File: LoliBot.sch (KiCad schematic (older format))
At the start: 37 parts, among them J1 LOLINBATT, J10 LEFT-MOTOR, J11 REFLECT_, J12 MECH, J13 MECH, J14 MECH, J15 MECH, J16 MECH, J17 MECH, J18 MECH, J19 MECH, J2 APA106, J3 SERVO1, J4 RIGHT, J5 LEFT, J6 MPU-9250, J7 APA106, J8 APA106, J9 RIGHT-MOTOR, SW1 SPST, U1 LOLIN32-LITE, U2 RT9276, U3 L9110, U4 L9110

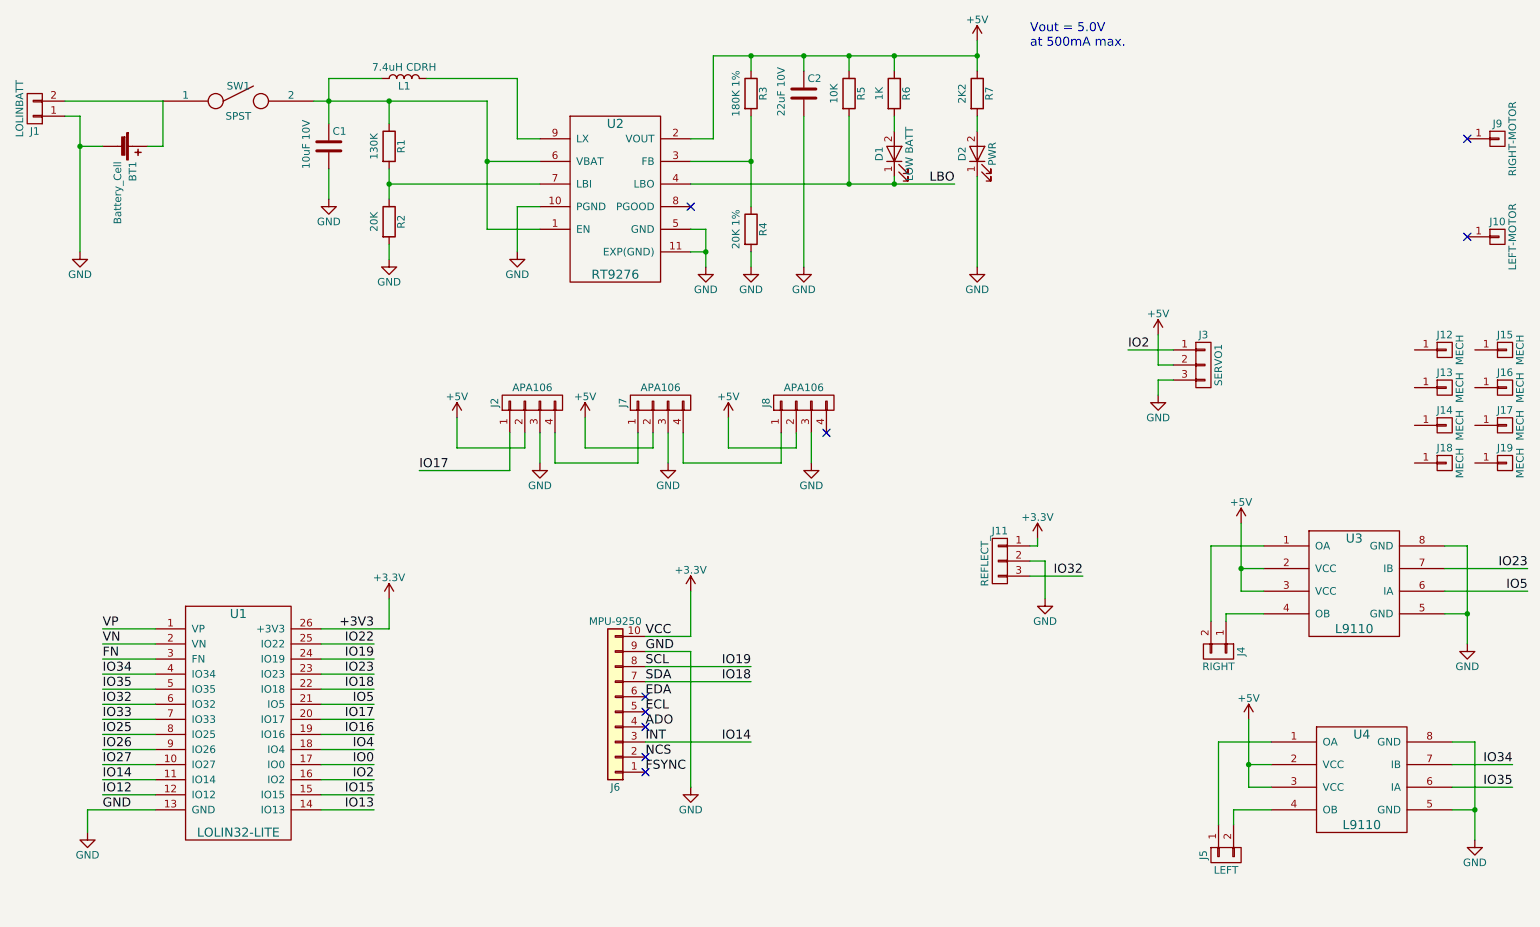
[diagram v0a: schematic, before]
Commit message: Pin reassignment.
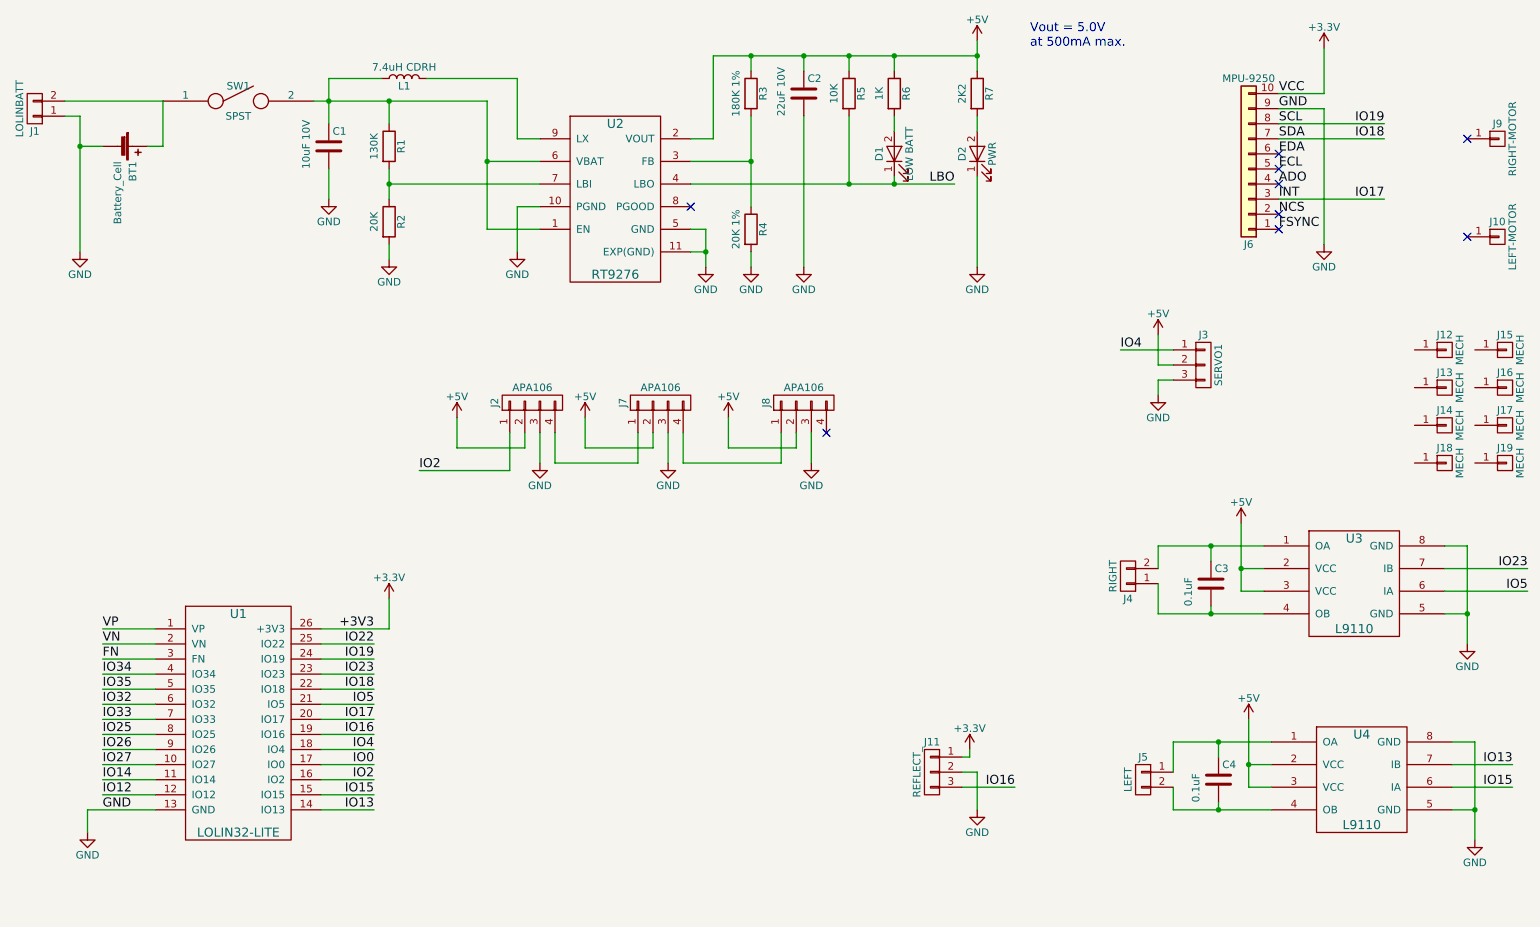
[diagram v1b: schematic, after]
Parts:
- added C3, C4: 0.1uF, Capacitors_SMD:C_0805_HandSoldering, symbol C
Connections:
- net INT: now also U1.20 (IO17); no longer U1.11 (IO14)
- net IO13: now also U4.7 (IB)
- net IO15: now also U4.6 (IA)
- net IO16: now also J11.3 (P3)
- net IO2: now also J2.1 (P1); no longer J3.1 (P1)
- net IO32: no longer J11.3 (P3)
- net IO34: no longer U4.7 (IB)
- net IO35: no longer U4.6 (IA)
- net IO4: now also J3.1 (P1)
- net at J4.2 (P2), U3.1 (OA): now also C3.1
- net at J4.1 (P1), U3.4 (OB): now also C3.2
- net at J5.1 (P1), U4.1 (OA): now also C4.1
- net at J5.2 (P2), U4.4 (OB): now also C4.2
- removed net IO17: J2.1 (P1), U1.20 (IO17)
- new net IO14: U1.11 (IO14)
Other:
- moved on the sheet: J11, J4, J5, J6
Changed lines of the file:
@@
 L CONN_01X02 J4
 U 1 1 59DBB5AA
-P 8800 4800
-F 0 "J4" H 8800 4950 50  0000 C CNN
-F 1 "RIGHT" V 8900 4800 50  0000 C CNN
-F 2 "Pin_Headers:Pin_Header_Straight_1x02_Pitch2.00mm" H 8800 4800 50  0001 C CNN
-F 3 "" H 8800 4800 50  0001 C CNN
-	1    8800 4800
-	0    1    1    0
+P 8200 4300
+F 0 "J4" H 8200 4450 50  0000 C CNN
+F 1 "RIGHT" V 8300 4300 50  0000 C CNN
+F 2 "Pin_Headers:Pin_Header_Straight_1x02_Pitch2.00mm" H 8200 4300 50  0001 C CNN
+F 3 "" H 8200 4300 50  0001 C CNN
+	1    8200 4300
+	-1   0    0    1
 $EndComp
 $Comp
@@
 L CONN_01X02 J5
 U 1 1 59DBCDBD
-P 8850 6150
-F 0 "J5" H 8850 6300 50  0000 C CNN
-F 1 "LEFT" V 8950 6150 50  0000 C CNN
-F 2 "Pin_Headers:Pin_Header_Straight_1x02_Pitch2.00mm" H 8850 6150 50  0001 C CNN
-F 3 "" H 8850 6150 50  0001 C CNN
-	1    8850 6150
-	0    -1   1    0
+P 8300 5650
+F 0 "J5" H 8300 5800 50  0000 C CNN
+F 1 "LEFT" V 8400 5650 50  0000 C CNN
+F 2 "Pin_Headers:Pin_Header_Straight_1x02_Pitch2.00mm" H 8300 5650 50  0001 C CNN
+F 3 "" H 8300 5650 50  0001 C CNN
+	1    8300 5650
+	-1   0    0    -1
 $EndComp
 $Comp
@@
 	9150 5550 9000 5550
 Connection ~ 9000 5550
-Text Label 10750 5550 2    60   ~ 0
-IO34
-Text Label 10750 5700 2    60   ~ 0
-IO35
 $Comp
 L CONN_01X03 J3
@@
 	8400 3000 8500 3000
 Wire Wire Line
-	8500 2800 8200 2800
-Text Label 8200 2800 0    60   ~ 0
-IO2
+	8500 2800 8150 2800
 Wire Wire Line
 	1750 4650 1400 4650
@@
 L Conn_01x10 J6
 U 1 1 59E28CBB
-P 4800 5200
-F 0 "J6" H 4800 5700 50  0000 C CNN
-F 1 "MPU-9250" H 4800 4600 50  0000 C CNN
-F 2 "Pin_Headers:Pin_Header_Straight_1x10_Pitch2.54mm" H 4800 5200 50  0001 C CNN
-F 3 "" H 4800 5200 50  0001 C CNN
-	1    4800 5200
+P 9000 1600
+F 0 "J6" H 9000 2100 50  0000 C CNN
+F 1 "MPU-9250" H 9000 1000 50  0000 C CNN
+F 2 "Pin_Headers:Pin_Header_Straight_1x10_Pitch2.54mm" H 9000 1600 50  0001 C CNN
+F 3 "" H 9000 1600 50  0001 C CNN
+	1    9000 1600
 	-1   0    0    1
 $EndComp
-Text Label 5000 4700 0    60   ~ 0
+Text Label 9200 1100 0    60   ~ 0
 VCC
-Text Label 5000 4800 0    60   ~ 0
+Text Label 9200 1200 0    60   ~ 0
 GND
-Text Label 5000 4900 0    60   ~ 0
+Text Label 9200 1300 0    60   ~ 0
 SCL
-Text Label 5000 5000 0    60   ~ 0
+Text Label 9200 1400 0    60   ~ 0
 SDA
-Text Label 5000 5100 0    60   ~ 0
+Text Label 9200 1500 0    60   ~ 0
 EDA
-Text Label 5000 5200 0    60   ~ 0
+Text Label 9200 1600 0    60   ~ 0
 ECL
-Text Label 5000 5300 0    60   ~ 0
+Text Label 9200 1700 0    60   ~ 0
 ADO
-Text Label 5000 5400 0    60   ~ 0
+Text Label 9200 1800 0    60   ~ 0
 INT
-Text Label 5000 5500 0    60   ~ 0
+Text Label 9200 1900 0    60   ~ 0
 NCS
-Text Label 5000 5600 0    60   ~ 0
+Text Label 9200 2000 0    60   ~ 0
 FSYNC
 $Comp
 L +3.3V #PWR020
 U 1 1 59E28F97
-P 5300 4400
-F 0 "#PWR020" H 5300 4250 50  0001 C CNN
-F 1 "+3.3V" H 5300 4540 50  0000 C CNN
-F 2 "" H 5300 4400 50  0001 C CNN
-F 3 "" H 5300 4400 50  0001 C CNN
-	1    5300 4400
-	1    0    0    -1
-$EndComp
-Wire Wire Line
-	5000 4700 5300 4700
-Wire Wire Line
-	5300 4700 5300 4400
+P 9500 800
+F 0 "#PWR020" H 9500 650 50  0001 C CNN
+F 1 "+3.3V" H 9500 940 50  0000 C CNN
+F 2 "" H 9500 800 50  0001 C CNN
+F 3 "" H 9500 800 50  0001 C CNN
+	1    9500 800
+	1    0    0    -1
+$EndComp
+Wire Wire Line
+	9200 1100 9500 1100
+Wire Wire Line
+	9500 1100 9500 800
 $Comp
 L GND #PWR021
 U 1 1 59E29073
-P 5300 5700
-F 0 "#PWR021" H 5300 5450 50  0001 C CNN
-F 1 "GND" H 5300 5550 50  0000 C CNN
-F 2 "" H 5300 5700 50  0001 C CNN
-F 3 "" H 5300 5700 50  0001 C CNN
-	1    5300 5700
-	1    0    0    -1
-$EndComp
-Wire Wire Line
-	5000 4800 5300 4800
-Wire Wire Line
-	5300 4800 5300 5700
-Wire Wire Line
-	5000 4900 5700 4900
-Wire Wire Line
-	5000 5000 5700 5000
-Text Label 5700 4900 2    60   ~ 0
+P 9500 2100
+F 0 "#PWR021" H 9500 1850 50  0001 C CNN
+F 1 "GND" H 9500 1950 50  0000 C CNN
+F 2 "" H 9500 2100 50  0001 C CNN
+F 3 "" H 9500 2100 50  0001 C CNN
+	1    9500 2100
+	1    0    0    -1
+$EndComp
+Wire Wire Line
+	9200 1200 9500 1200
+Wire Wire Line
+	9500 1200 9500 2100
+Wire Wire Line
+	9200 1300 9900 1300
+Wire Wire Line
+	9200 1400 9900 1400
+Text Label 9900 1300 2    60   ~ 0
 IO19
-Text Label 5700 5000 2    60   ~ 0
+Text Label 9900 1400 2    60   ~ 0
 IO18
 Wire Wire Line
-	5000 5400 5700 5400
-Text Label 5700 5400 2    60   ~ 0
-IO14
-NoConn ~ 5000 5600
-NoConn ~ 5000 5500
-NoConn ~ 5000 5300
-NoConn ~ 5000 5200
-NoConn ~ 5000 5100
+	9200 1800 9900 1800
+NoConn ~ 9200 2000
+NoConn ~ 9200 1900
+NoConn ~ 9200 1700
+NoConn ~ 9200 1600
+NoConn ~ 9200 1500
 $Comp
 L CONN_01X04 J7
@@
 Wire Wire Line
 	3500 3600 4100 3600
-Text Label 3500 3600 0    60   ~ 0
-IO17
 $Comp
 L +5V #PWR022
@@
 L CONN_01X03 J11
 U 1 1 59F9CFA7
-P 7350 4200
-F 0 "J11" H 7350 4400 50  0000 C CNN
-F 1 "REFLECT_" V 7450 4200 50  0000 C CNN
-F 2 "Pin_Headers:Pin_Header_Straight_1x03_Pitch2.54mm" H 7350 4200 50  0001 C CNN
-F 3 "" H 7350 4200 50  0001 C CNN
-	1    7350 4200
+P 6900 5600
+F 0 "J11" H 6900 5800 50  0000 C CNN
+F 1 "REFLECT_" V 7000 5600 50  0000 C CNN
+F 2 "Pin_Headers:Pin_Header_Straight_1x03_Pitch2.54mm" H 6900 5600 50  0001 C CNN
+F 3 "" H 6900 5600 50  0001 C CNN
+	1    6900 5600
 	-1   0    0    -1
 $EndComp
@@
 L +3.3V #PWR026
 U 1 1 59F9D53B
-P 7600 4050
-F 0 "#PWR026" H 7600 3900 50  0001 C CNN
-F 1 "+3.3V" H 7600 4190 50  0000 C CNN
-F 2 "" H 7600 4050 50  0001 C CNN
-F 3 "" H 7600 4050 50  0001 C CNN
-	1    7600 4050
+P 7150 5450
+F 0 "#PWR026" H 7150 5300 50  0001 C CNN
+F 1 "+3.3V" H 7150 5590 50  0000 C CNN
+F 2 "" H 7150 5450 50  0001 C CNN
+F 3 "" H 7150 5450 50  0001 C CNN
+	1    7150 5450
 	1    0    0    -1
 $EndComp
@@
 L GND #PWR027
 U 1 1 59F9DB04
-P 7650 4450
-F 0 "#PWR027" H 7650 4200 50  0001 C CNN
-F 1 "GND" H 7650 4300 50  0000 C CNN
-F 2 "" H 7650 4450 50  0001 C CNN
-F 3 "" H 7650 4450 50  0001 C CNN
-	1    7650 4450
-	1    0    0    -1
-$EndComp
-Wire Wire Line
-	7550 4100 7600 4100
-Wire Wire Line
-	7600 4100 7600 4050
-Wire Wire Line
-	7550 4200 7650 4200
-Wire Wire Line
-	7650 4200 7650 4450
-Text Label 7900 4300 2    60   ~ 0
-IO32
-Wire Wire Line
-	7550 4300 7900 4300
+P 7200 5850
+F 0 "#PWR027" H 7200 5600 50  0001 C CNN
+F 1 "GND" H 7200 5700 50  0000 C CNN
+F 2 "" H 7200 5850 50  0001 C CNN
+F 3 "" H 7200 5850 50  0001 C CNN
+	1    7200 5850
+	1    0    0    -1
+$EndComp
+Wire Wire Line
+	7100 5500 7150 5500
+Wire Wire Line
+	7150 5500 7150 5450
+Wire Wire Line
+	7100 5600 7200 5600
+Wire Wire Line
+	7200 5600 7200 5850
+Wire Wire Line
+	7100 5700 7450 5700
 $Comp
 L CONN_01X01 J19
@@
 $EndComp
 Wire Wire Line
-	8850 4600 8850 4550
-Wire Wire Line
-	8850 4550 9100 4550
-Wire Wire Line
-	9100 4100 8750 4100
-Wire Wire Line
-	8750 4100 8750 4600
-Wire Wire Line
-	9150 5850 8900 5850
-Wire Wire Line
-	8900 5850 8900 5950
-Wire Wire Line
-	9150 5400 8800 5400
-Wire Wire Line
-	8800 5400 8800 5950
+	8400 4550 9100 4550
+Wire Wire Line
+	8400 4100 9100 4100
+Wire Wire Line
+	8500 5850 9150 5850
+Wire Wire Line
+	8500 5400 9150 5400
+Text Label 10750 5550 2    60   ~ 0
+IO13
+Text Label 9900 1800 2    60   ~ 0
+IO17
+Text Label 7450 5700 2    60   ~ 0
+IO16
+Text Label 8150 2800 0    60   ~ 0
+IO4
+Text Label 3500 3600 0    60   ~ 0
+IO2
+Text Label 10750 5700 2    60   ~ 0
+IO15
+$Comp
+L C C3
+U 1 1 5A0F0864
+P 8750 4350
+F 0 "C3" H 8775 4450 50  0000 L CNN
+F 1 "0.1uF" V 8600 4200 50  0000 L CNN
+F 2 "Capacitors_SMD:C_0805_HandSoldering" H 8788 4200 50  0001 C CNN
+F 3 "" H 8750 4350 50  0001 C CNN
+	1    8750 4350
+	1    0    0    -1
+$EndComp
+$Comp
+L C C4
+U 1 1 5A0F0D3D
+P 8800 5650
+F 0 "C4" H 8825 5750 50  0000 L CNN
+F 1 "0.1uF" V 8650 5500 50  0000 L CNN
+F 2 "Capacitors_SMD:C_0805_HandSoldering" H 8838 5500 50  0001 C CNN
+F 3 "" H 8800 5650 50  0001 C CNN
+	1    8800 5650
+	1    0    0    -1
+$EndComp
+Wire Wire Line
+	8800 5400 8800 5500
+Wire Wire Line
+	8800 5850 8800 5800
+Wire Wire Line
+	8500 5850 8500 5700
+Connection ~ 8800 5850
+Wire Wire Line
+	8500 5400 8500 5600
+Connection ~ 8800 5400
+Wire Wire Line
+	8750 4500 8750 4550
+Wire Wire Line
+	8750 4100 8750 4200
+Wire Wire Line
+	8400 4250 8400 4100
+Connection ~ 8750 4100
+Wire Wire Line
+	8400 4350 8400 4550
+Connection ~ 8750 4550
 $EndSCHEMATC

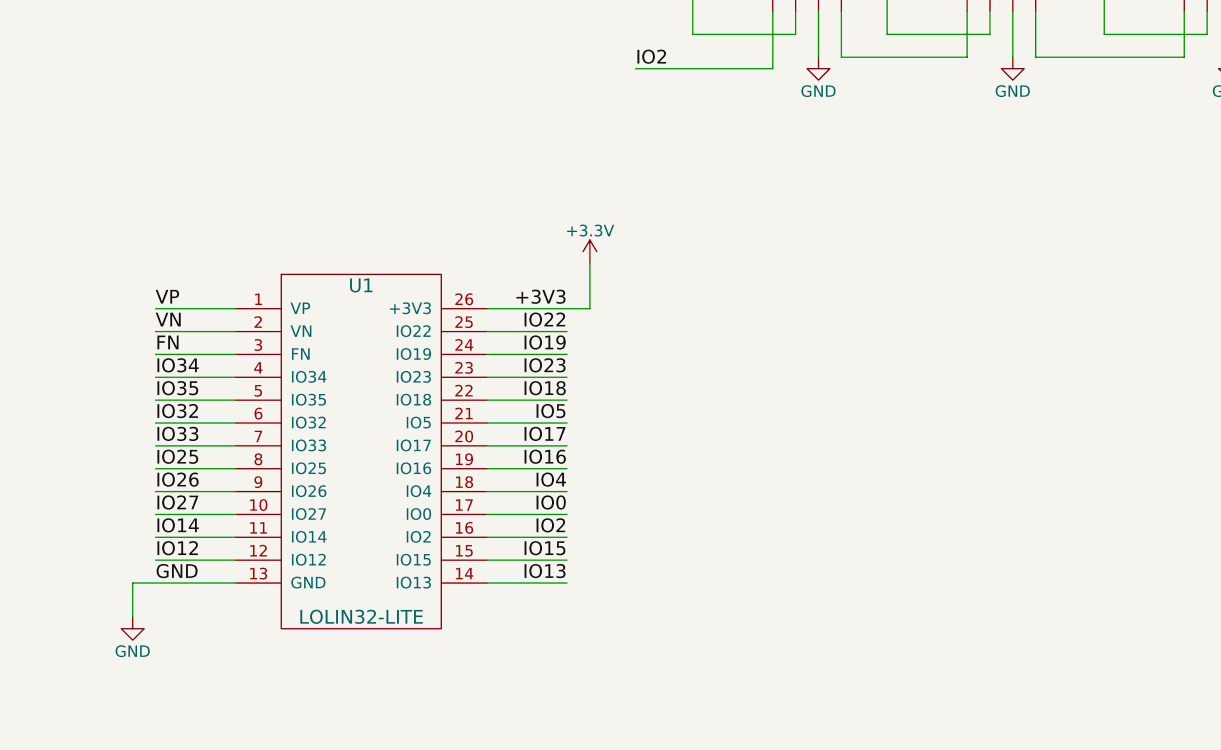
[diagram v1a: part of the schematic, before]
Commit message: Added expansion ports
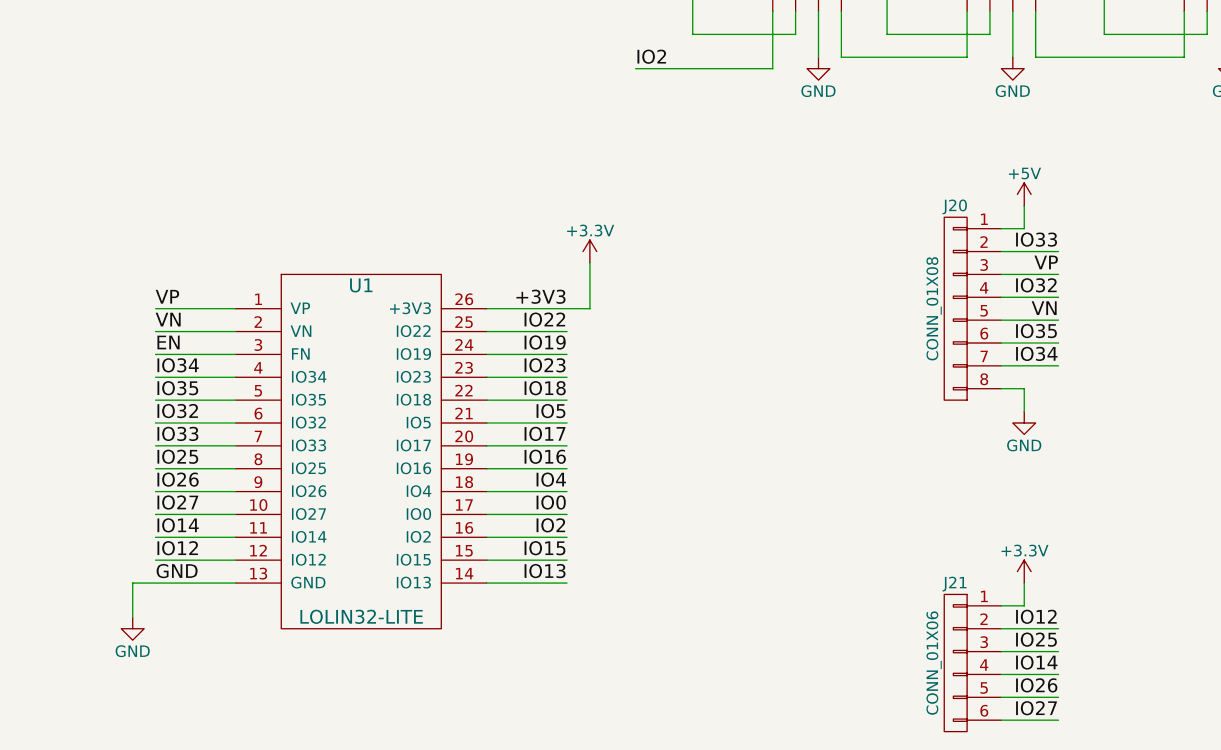
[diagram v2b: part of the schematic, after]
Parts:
- added J20: CONN_01X08, Pin_Headers:Pin_Header_Straight_2x04_Pitch2.54mm, symbol CONN_01X08
- added J21: CONN_01X06, Pin_Headers:Pin_Header_Straight_2x03_Pitch2.54mm, symbol CONN_01X06
- U3, U4: footprint Housings_DIP:DIP-8_W7.62mm -> Housings_SOIC:SOIC-8_3.9x4.9mm_Pitch1.27mm
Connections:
- net +3V3: now also J21.1 (P1)
- net +5V: now also J20.1 (P1)
- net GND: now also J20.8 (P8)
- net IO12: now also J21.2 (P2)
- net IO14: now also J21.4 (P4)
- net IO25: now also J21.3 (P3)
- net IO26: now also J21.5 (P5)
- net IO27: now also J21.6 (P6)
- net IO32: now also J20.4 (P4)
- net IO33: now also J20.2 (P2)
- net IO34: now also J20.7 (P7)
- net IO35: now also J20.6 (P6)
- net VN: now also J20.5 (P5)
- net VP: now also J20.3 (P3)
- net FN renamed EN
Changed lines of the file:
@@
 F 0 "U3" H 9700 4550 60  0000 C CNN
 F 1 "L9110" H 9700 3950 60  0000 C CNN
-F 2 "Housings_DIP:DIP-8_W7.62mm" H 9700 4300 60  0001 C CNN
+F 2 "Housings_SOIC:SOIC-8_3.9x4.9mm_Pitch1.27mm" H 9700 4300 60  0001 C CNN
 F 3 "" H 9700 4300 60  0000 C CNN
 	1    9700 4300
@@
 F 0 "U4" H 9750 5850 60  0000 C CNN
 F 1 "L9110" H 9750 5250 60  0000 C CNN
-F 2 "Housings_DIP:DIP-8_W7.62mm" H 9750 5600 60  0001 C CNN
+F 2 "Housings_SOIC:SOIC-8_3.9x4.9mm_Pitch1.27mm" H 9750 5600 60  0001 C CNN
 F 3 "" H 9750 5600 60  0000 C CNN
 	1    9750 5600
@@
 	1750 4850 1400 4850
 Text Label 1400 4850 0    60   ~ 0
-FN
+EN
 Wire Wire Line
 	1750 4950 1400 4950
@@
 	8400 4350 8400 4550
 Connection ~ 8750 4550
+$Comp
+L CONN_01X08 J20
+U 1 1 5A117712
+P 4900 4650
+F 0 "J20" H 4900 5100 50  0000 C CNN
+F 1 "CONN_01X08" V 5000 4650 50  0000 C CNN
+F 2 "Pin_Headers:Pin_Header_Straight_2x04_Pitch2.54mm" H 4900 4650 50  0001 C CNN
+F 3 "" H 4900 4650 50  0001 C CNN
+	1    4900 4650
+	-1   0    0    -1
+$EndComp
+$Comp
+L +3.3V #PWR028
+U 1 1 5A117D1F
+P 5200 5850
+F 0 "#PWR028" H 5200 5700 50  0001 C CNN
+F 1 "+3.3V" H 5200 5990 50  0000 C CNN
+F 2 "" H 5200 5850 50  0001 C CNN
+F 3 "" H 5200 5850 50  0001 C CNN
+	1    5200 5850
+	1    0    0    -1
+$EndComp
+Wire Wire Line
+	5100 4300 5200 4300
+Wire Wire Line
+	5200 4300 5200 4200
+Text Label 5350 4500 2    60   ~ 0
+VP
+Text Label 5350 4700 2    60   ~ 0
+VN
+Text Label 5350 4900 2    60   ~ 0
+IO34
+Text Label 5350 4800 2    60   ~ 0
+IO35
+Text Label 5350 4600 2    60   ~ 0
+IO32
+Text Label 5350 4400 2    60   ~ 0
+IO33
+$Comp
+L GND #PWR029
+U 1 1 5A1181BF
+P 5200 5100
+F 0 "#PWR029" H 5200 4850 50  0001 C CNN
+F 1 "GND" H 5200 4950 50  0000 C CNN
+F 2 "" H 5200 5100 50  0001 C CNN
+F 3 "" H 5200 5100 50  0001 C CNN
+	1    5200 5100
+	1    0    0    -1
+$EndComp
+Wire Wire Line
+	5100 5000 5200 5000
+Wire Wire Line
+	5200 5000 5200 5100
+Wire Wire Line
+	5100 4400 5350 4400
+Wire Wire Line
+	5100 4500 5350 4500
+Wire Wire Line
+	5350 4600 5100 4600
+Wire Wire Line
+	5100 4700 5350 4700
+Wire Wire Line
+	5350 4800 5100 4800
+Wire Wire Line
+	5350 4900 5100 4900
+$Comp
+L +5V #PWR030
+U 1 1 5A11954A
+P 5200 4200
+F 0 "#PWR030" H 5200 4050 50  0001 C CNN
+F 1 "+5V" H 5200 4340 50  0000 C CNN
+F 2 "" H 5200 4200 50  0001 C CNN
+F 3 "" H 5200 4200 50  0001 C CNN
+	1    5200 4200
+	1    0    0    -1
+$EndComp
+Text Label 5350 6150 2    60   ~ 0
+IO25
+Text Label 5350 6350 2    60   ~ 0
+IO26
+Text Label 5350 6450 2    60   ~ 0
+IO27
+Text Label 5350 6250 2    60   ~ 0
+IO14
+Text Label 5350 6050 2    60   ~ 0
+IO12
+$Comp
+L CONN_01X06 J21
+U 1 1 5A11A25A
+P 4900 6200
+F 0 "J21" H 4900 6550 50  0000 C CNN
+F 1 "CONN_01X06" V 5000 6200 50  0000 C CNN
+F 2 "Pin_Headers:Pin_Header_Straight_2x03_Pitch2.54mm" H 4900 6200 50  0001 C CNN
+F 3 "" H 4900 6200 50  0001 C CNN
+	1    4900 6200
+	-1   0    0    -1
+$EndComp
+Wire Wire Line
+	5100 5950 5200 5950
+Wire Wire Line
+	5200 5950 5200 5850
+Wire Wire Line
+	5100 6050 5350 6050
+Wire Wire Line
+	5350 6150 5100 6150
+Wire Wire Line
+	5100 6250 5350 6250
+Wire Wire Line
+	5350 6350 5100 6350
+Wire Wire Line
+	5100 6450 5350 6450
 $EndSCHEMATC
